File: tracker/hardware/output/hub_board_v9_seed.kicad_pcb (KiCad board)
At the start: 4 copper layers, 70 x 70 mm, 39 parts, among them U1 ESP32-S3-WROOM-1U-N8R8, U2 LoRa2021F33-2G4, U3 LoRa2021_Castellated, U4 SX1280, U5 MAX-M10S, U6 MS5611-01BA, U7 TPS7A02

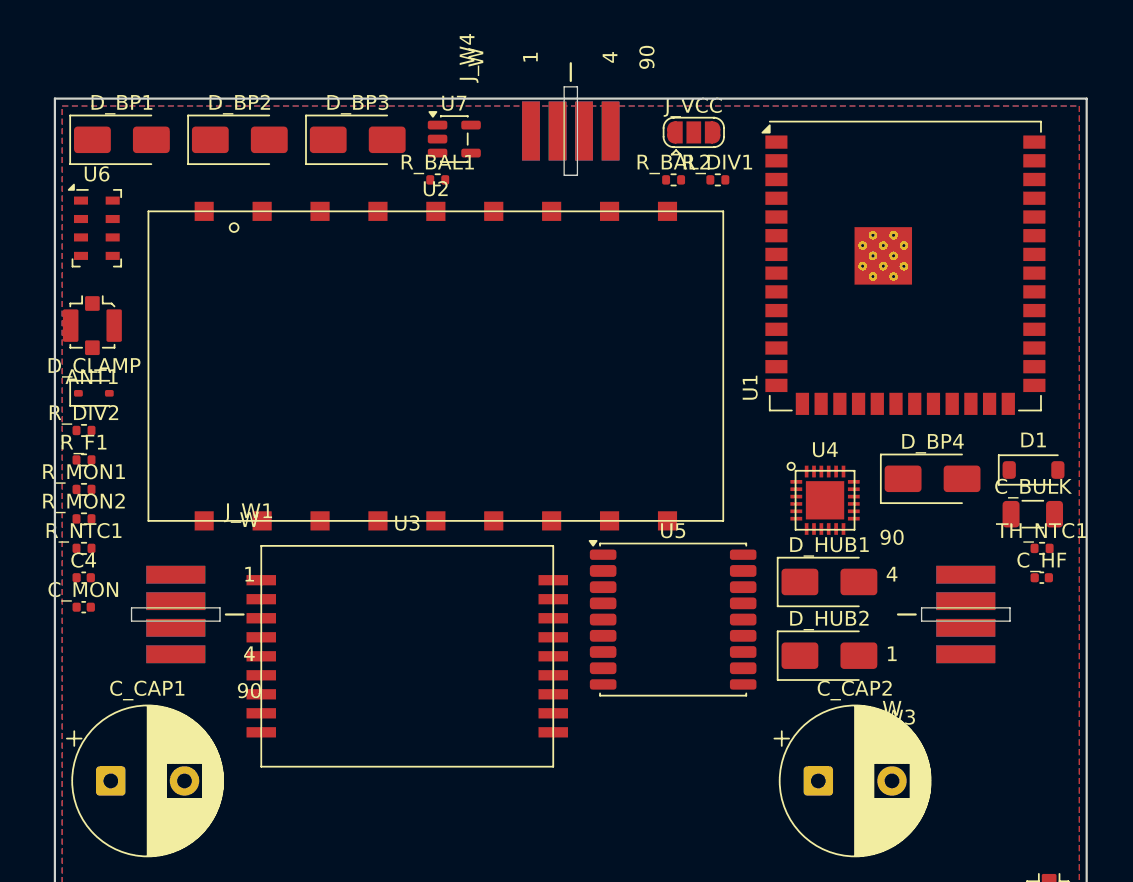
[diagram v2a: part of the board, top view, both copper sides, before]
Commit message: feat(hub): 44/44 PLACED -- the 7-missing-parts defect is CLOSED at the board level; gate now names the stale package
THE DEFECT THAT REACHED THE ORDER PACKAGE IS FIXED. Rebuilt with --publish after the symbol surgery:
    components : 44 on netlist / 44 placed / 0 with an EMPTY footprint field   (was 46/39/7)
    outline    : 70.0 x 70.0 mm
    krt placer : parts_moved 17, pad_overlap_pairs 0, pad_intersection_pairs 0
    frozen board: tracker/hardware/hub_board_v9.kicad_pcb  sha256 c0ff66dc...
U_CUT1-4 (SN74LVC1G373DBVR, SOT-23-6) and U_HUB_CVT (BQ25504RGTR, VQFN-16) are now physically placed.
PVA1/PVA2 correctly left the board.

I ALSO FIXED A CONFLATION IN MY OWN GATE THAT WAS HIDING WHICH LINK WAS BROKEN.
Section C compared the netlist against the PACKAGED board only, so when the committed board had been
regenerated to 44/44 while the packaged (routed) artifact still carried 39, it reported ONE opaque
failure. There are two distinct links and they are now checked separately:
    C1  netlist  ->  the single-writer's COMMITTED board   (is the design placed at all?)
    C2  committed ->  the PACKAGED board                   (is the order package current?)
RESULT: C1 PASSES (netlist declares 44, committed board carries 44). C2 FAILS CORRECTLY, naming the
exact staleness: "the packaged board is STALE: it lacks ['U_CUT1','U_CUT2','U_CUT3','U_CUT4',
'U_HUB_CVT']" and saying to route the committed board, re-emit BOM/CPL/gerbers, and copy it into the
package. A check that names the broken link is worth more than one that reports a symptom.

GATE: test_netlist_integrity.py 14 pass, 1 FAIL -- and the one failure is a REAL, ACTIONABLE state,
not a defect in the design. Sections A (empty footprint) and B (unresolvable footprint) PASS, and C1
PASSES. test_order_package_consistency.py remains 5 pass / 1 FAIL (the three-slot gap, awaiting Site C).

WHAT REMAINS FOR THE HUB ORDER PACKAGE: route the committed 44-part board, then re-emit the BOM and
CPL and the gerbers and copy th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
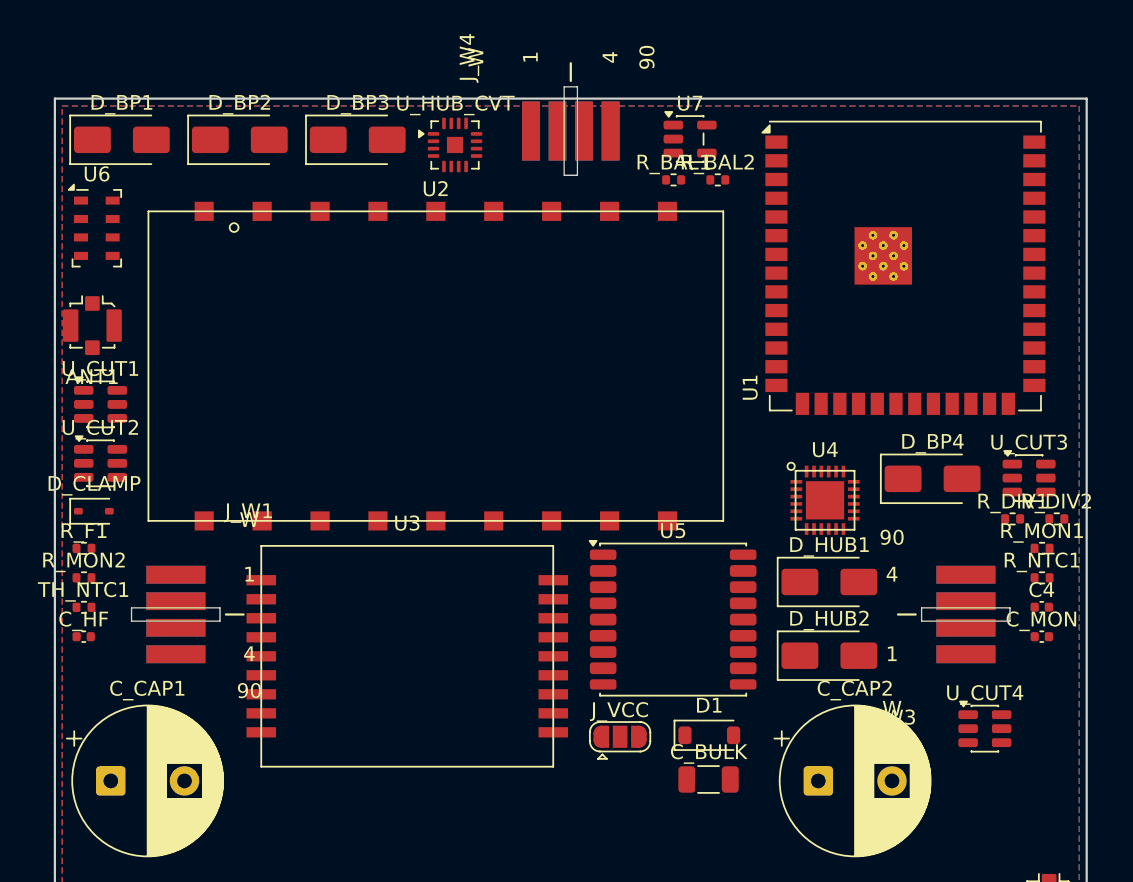
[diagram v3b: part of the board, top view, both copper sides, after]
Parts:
- added U_CUT1: SN74LVC1G373DBVR, Package_TO_SOT_SMD:SOT-23-6, F.Cu at (3.10, 20.7)
- added U_CUT2: SN74LVC1G373DBVR, Package_TO_SOT_SMD:SOT-23-6, F.Cu at (3.10, 24.7)
- added U_CUT3: SN74LVC1G373DBVR, Package_TO_SOT_SMD:SOT-23-6, F.Cu at (66.1, 25.7)
- added U_CUT4: SN74LVC1G373DBVR, Package_TO_SOT_SMD:SOT-23-6, F.Cu at (63.1, 42.7)
- added U_HUB_CVT: BQ25504RGTR, Package_DFN_QFN:VQFN-16-1EP_3x3mm_P0.5mm_EP1.1x1.1mm, F.Cu at (27.1, 3.15)
- moved R_DIV2 66.3 mm to (68.0, 28.5)
- moved C_HF 65.1 mm to (1.96, 36.5)
- moved R_MON1 65.1 mm to (67.0, 30.5)
- moved TH_NTC1 65.1 mm to (1.98, 34.5)
- moved C4 65.0 mm to (67.0, 34.5)
- moved C_MON 65.0 mm to (67.0, 36.5)
- moved R_NTC1 65.0 mm to (67.0, 32.5)
- moved J_VCC 41.3 mm to (38.3, 43.3)
- moved R_DIV1 30.5 mm to (65.0, 28.5)
- moved C_BULK 28.4 mm to (44.3, 46.2)
- moved D1 28.4 mm to (44.4, 43.2)
- moved R_BAL1 16.0 mm to (42.0, 5.51)
- moved U7 16.0 mm to (43.1, 2.75)
- moved D_CLAMP 8.00 mm to (2.65, 28.0)
- moved R_F1 6.00 mm to (1.98, 30.5)
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
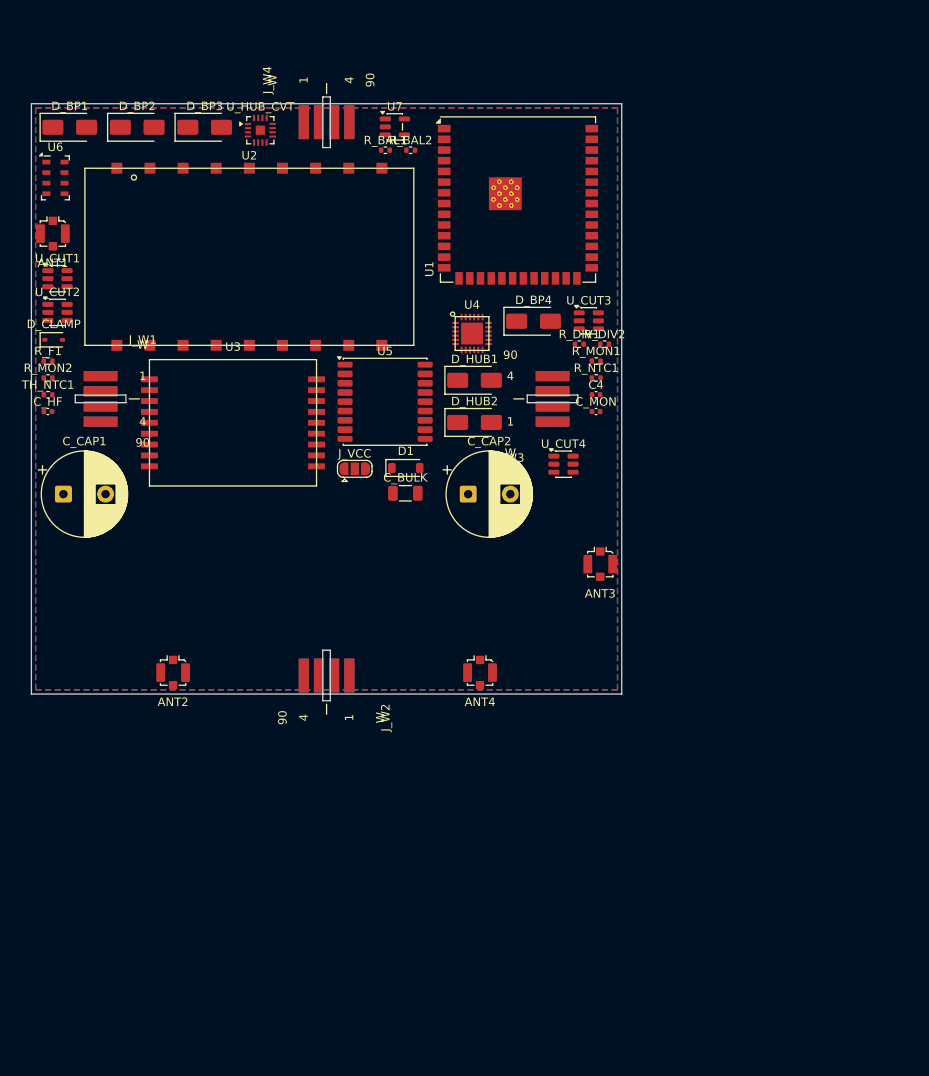
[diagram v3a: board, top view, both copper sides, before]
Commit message: fix(hw): regenerate the hub placement -- all four wing slots now reach their edge
Regenerated with the corrected seat rule:

  KRT_DIR=/data/repos/KiCadRoutingTools ~/venvs/kicad/bin/python       tracker/hardware/build_hub_board_v9.py       --out tracker/hardware/output/hub_board_v9_seed.kicad_pcb --publish

seed sha256 7eb1b7dce0fe38fa...  -> verify_wing_interfaces.py EXIT 0
KRT lap sha256 d8b23136d88e2e51... -> verify_wing_interfaces.py EXIT 0

OFFSET: 5.20 mm before -> 0.00 mm after (derived from the corrected rotations).

Slot union bbox per tab (absolute mm), outline Edge.Cuts bbox -0.07..70.08 both axes:
  J_W1 west  rot   0  x -0.03.. 6.03  y 34.52..35.48  reaches LEFT   edge
  J_W2 north rot  90  x 34.52..35.48  y 63.98..70.03  reaches BOTTOM edge
  J_W3 east  rot 180  x 63.98..70.03  y 34.52..35.48  reaches RIGHT  edge
  J_W4 south rot 270  x 34.52..35.48  y -0.03.. 6.03  reaches TOP    edge
Every slot crosses its own edge by 0.03 mm; tolerance 0.30 mm.  Detector 1 -> 0.

CANONICAL BOARD DELIBERATELY NOT OVERWRITTEN. hub_board_v9.kicad_pcb is the
ROUTED board (834 tracks / 286 vias / 57-59 nets, promoted by ff87f4953).  The
builder is a PLACEMENT writer: its output has 0 tracks and 0 vias, and routing is
a separate step (fab_grade.sh -> KRT py_router/route.py).  Regenerating the
canonical path drops the routing and the repo's own gate refuses it:

  fab_readiness_guard.py --check -> REFUSING: tracks 0 < recorded 834

The reduction is a SIDE EFFECT, not intentional, so FAB_GUARD_ACK is not
appropriate and --no-verify is forbidden.  The canonical board is left intact at
sha256 e55a2946... (it still exits 1 on the detector -- the honest gate on it).

FOOTPRINT MOVE / CLEARANCE / ROUTING: KRT reports parts_moved 18,
pad_edge_conflicts unchanged at 16 (before and after), shortfall 8.0 mm both.
NO re-routing was performed.  See docs/fab/WING-INTERFACE-SEAT-RULE-FIX.md.
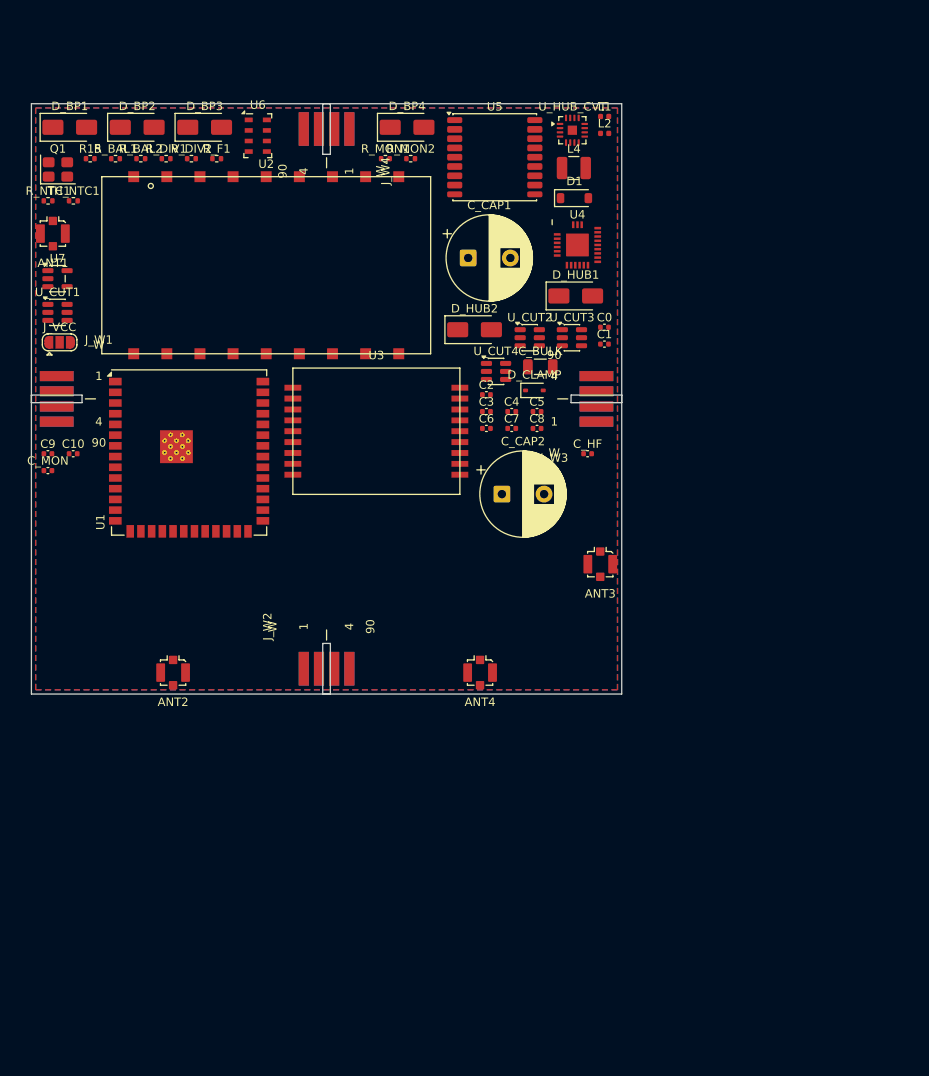
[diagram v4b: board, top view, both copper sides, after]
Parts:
- added C0: 0.8pF, Capacitor_SMD:C_0402_1005Metric, F.Cu at (68.0, 26.5)
- added C1: 1.2pF, Capacitor_SMD:C_0402_1005Metric, F.Cu at (68.0, 28.5)
- added C10: 100nF, Capacitor_SMD:C_0402_1005Metric, F.Cu at (4.96, 41.5)
- added C2: 1.2pF, Capacitor_SMD:C_0402_1005Metric, F.Cu at (54.0, 34.5)
- added C3: 100pF, Capacitor_SMD:C_0402_1005Metric, F.Cu at (54.0, 36.5)
- added C5: 10nF, Capacitor_SMD:C_0402_1005Metric, F.Cu at (60.0, 36.5)
- added C6: 10nF, Capacitor_SMD:C_0402_1005Metric, F.Cu at (54.0, 38.5)
- added C7: 0.5pF, Capacitor_SMD:C_0402_1005Metric, F.Cu at (57.0, 38.5)
- added C8: 100nF, Capacitor_SMD:C_0402_1005Metric, F.Cu at (60.0, 38.5)
- added C9: 470nF, Capacitor_SMD:C_0402_1005Metric, F.Cu at (1.96, 41.5)
- added L1: 3.0nH, Inductor_SMD:L_0402_1005Metric, F.Cu at (68.0, 1.51)
- added L2: 2.5nH, Inductor_SMD:L_0402_1005Metric, F.Cu at (68.0, 3.52)
- added L4: 15uH, Inductor_SMD:L_1210_3225Metric, F.Cu at (64.3, 7.62)
- added Q1: 52MHz, Crystal:Crystal_SMD_3225-4Pin_3.2x2.5mm, F.Cu at (3.15, 7.79)
- added R15: 0R, Resistor_SMD:R_0402_1005Metric, F.Cu at (6.97, 6.51)
- moved R_NTC1 68.3 mm to (1.98, 11.5)
- moved C_MON 65.4 mm to (1.96, 43.5)
- moved C_HF 64.2 mm to (66.0, 41.5)
- moved D_CLAMP 57.3 mm to (59.6, 34.0)
- moved U_CUT2 56.1 mm to (59.1, 27.7)
- moved C_CAP1 55.6 mm to (51.8, 18.3)
- moved R_DIV1 53.7 mm to (16.0, 6.51)
- moved R_DIV2 53.7 mm to (19.0, 6.51)
- moved R_MON2 50.2 mm to (45.0, 6.51)
- moved U1 49.2 mm to (18.7, 41.4)
- moved U7 43.9 mm to (3.10, 20.7)
- moved J_VCC 38.1 mm to (3.35, 28.3)
- moved D1 37.7 mm to (64.4, 11.2)
- moved U_HUB_CVT 37.0 mm to (64.1, 3.15)
- moved R_MON1 34.7 mm to (42.0, 6.51)
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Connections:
- U1 pad 35: /SX1280_ANT_SW -> (no net)
- U4 pad 1: +3V3 -> /SX1280_VR_PA
- U4 pad 10: /SX1280_DIO1 -> /SX1280_DIO3
- U4 pad 11: /SX1280_DIO2 -> /SX1280_VBAT_IO
- U4 pad 12: /SX1280_DIO3 -> /SX1280_VDD
- U4 pad 13: /SX1280_ANT_SW -> GND
- U4 pad 14: /ANT2_2G4_RANGE -> /SX1280_DCC_SW
- U4 pad 15: GND -> +3V3
- U4 pad 16: GND -> /SX1280_MISO
- U4 pad 17: GND -> /SX1280_MOSI
- U4 pad 18: GND -> /SX1280_SCK
- U4 pad 19: GND -> /SX1280_CS_N
- U4 pad 2: +3V3 -> /SX1280_VDD
- U4 pad 22: GND -> /SX1280_RF
- U4 pad 3: GND -> /SX1280_RESET_N
- U4 pad 4: /SX1280_RESET_N -> /SX1280_XTA
- U4 pad 5: /SX1280_BUSY -> GND
- U4 pad 6: /SX1280_CS_N -> /SX1280_XTB
- U4 pad 7: /SX1280_SCK -> /SX1280_BUSY
- U4 pad 8: /SX1280_MOSI -> /SX1280_DIO1
- U4 pad 9: /SX1280_MISO -> /SX1280_DIO2
